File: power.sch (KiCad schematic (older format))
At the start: 23 parts, among them P1 CONN_01X02, P2 CONN_01X02, P23 CONN_01X02, P24 CONN_01X02, P3 CONN_01X02, P4 CONN_01X02, U1 ST1S14PHR

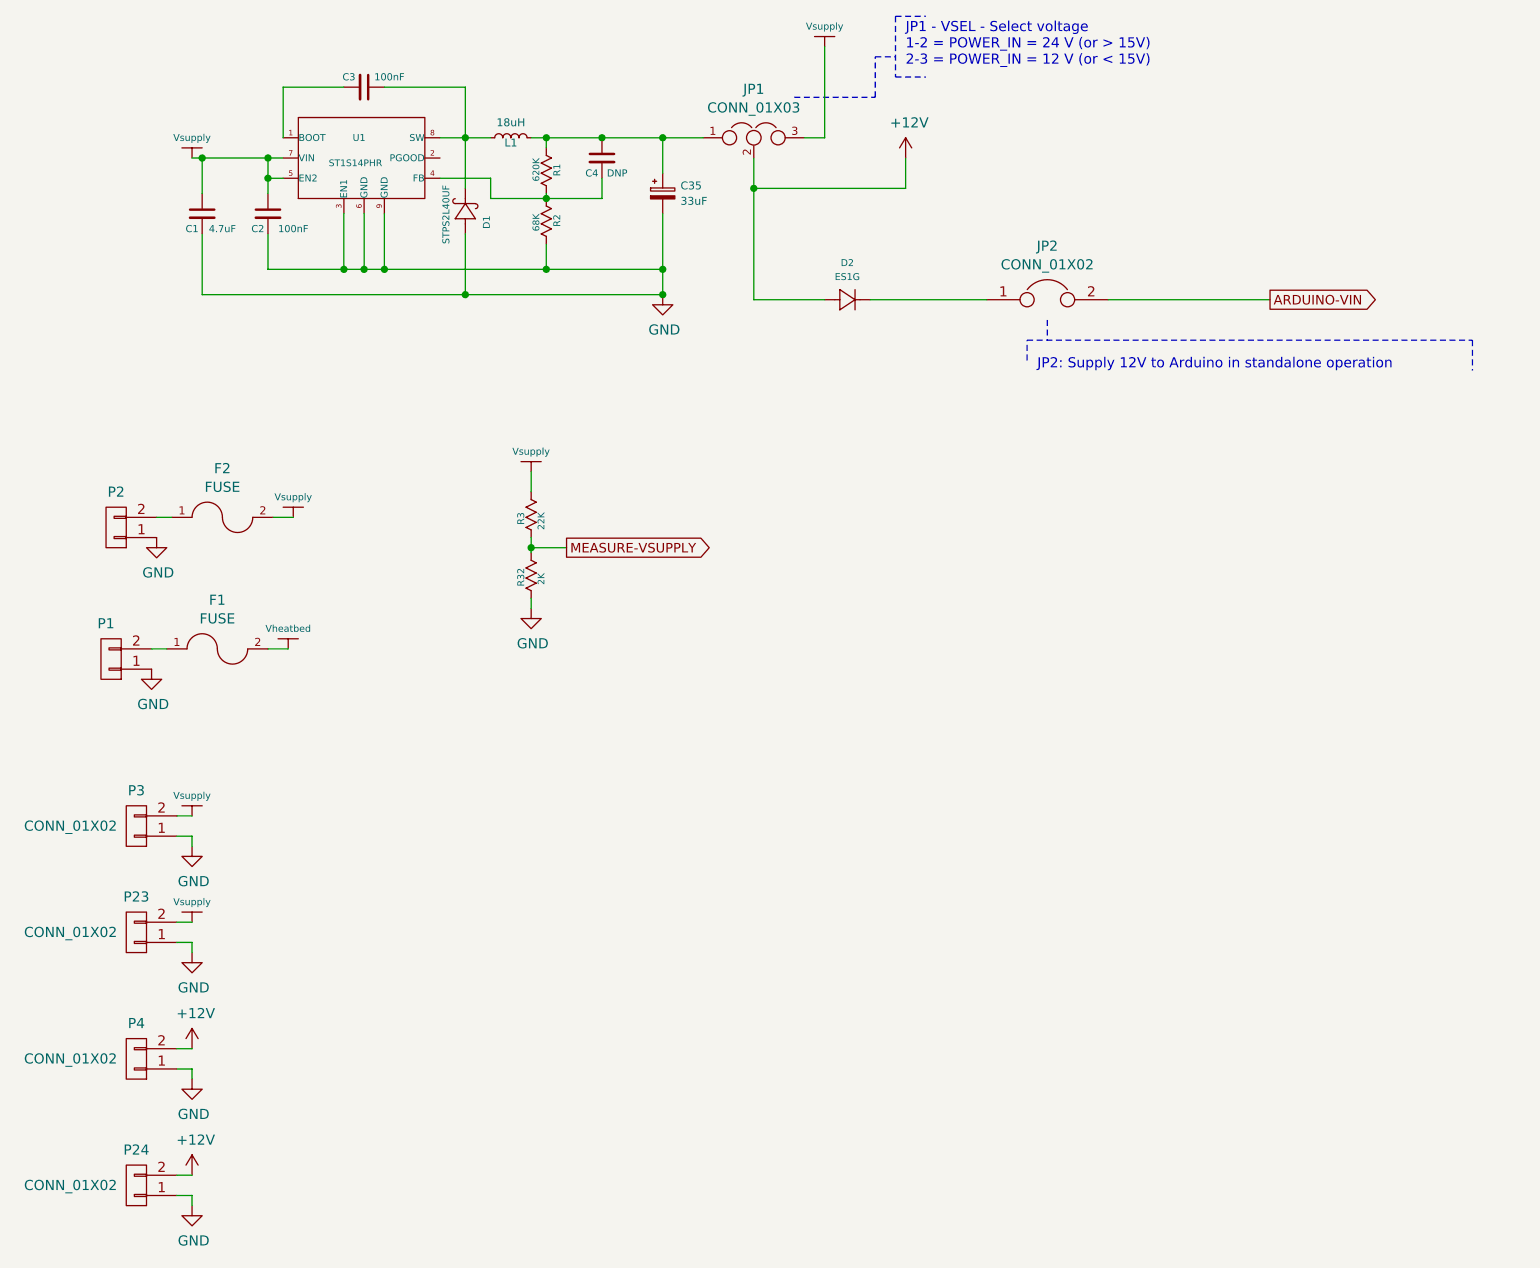
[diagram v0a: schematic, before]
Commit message: Removed jumper in arduino power line: arduino is now always powered when FireMC is powered
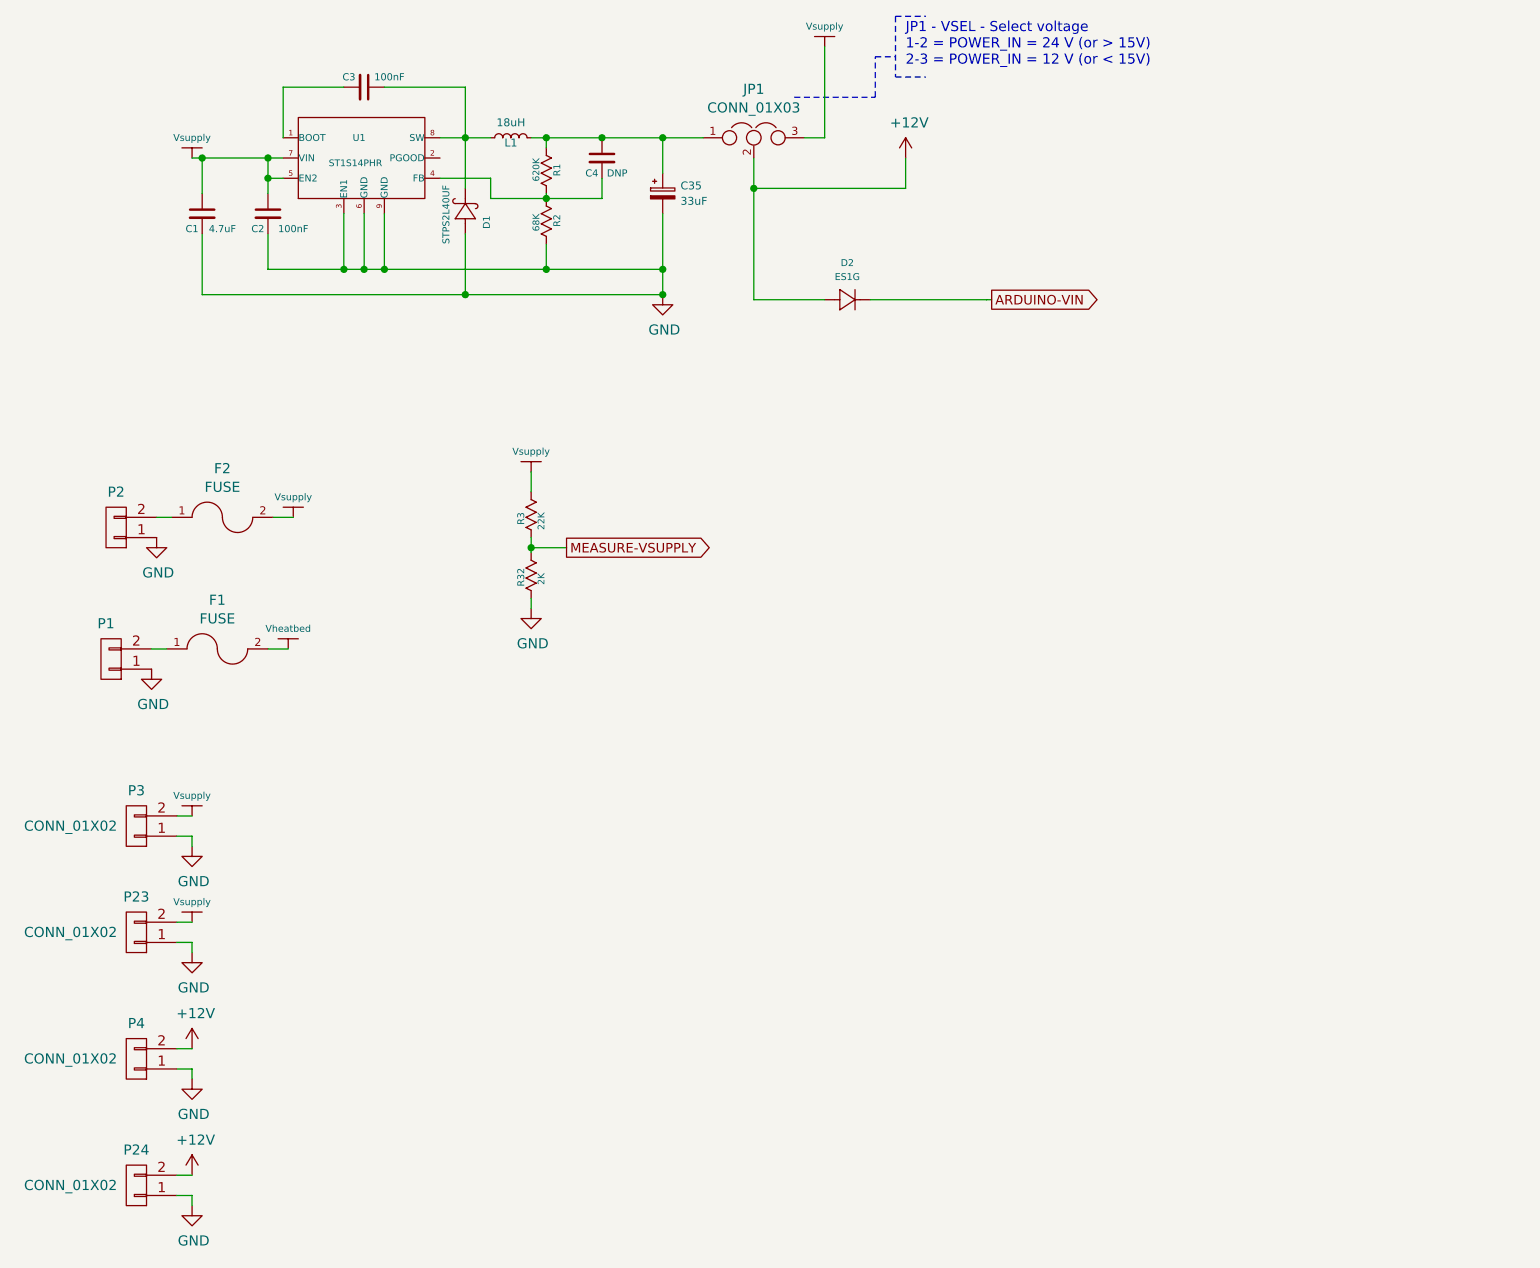
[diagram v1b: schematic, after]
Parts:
- removed JP2: CONN_01X02, headers:CON_HDR_1x2_2.54mm, symbol JUMPER
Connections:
- net ARDUINO-VIN: now also D2.1 (null)
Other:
- note removed: "JP2: Supply 12V to Arduino in standalone operation\n"
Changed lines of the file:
@@
 	5150 2075 4400 2075
 Wire Wire Line
-	6150 2625 6950 2625
+	5550 2625 5575 2625
 Wire Wire Line
 	5550 2625 4975 2625
@@
 Text Notes 5150 1475 0    50   ~ 0
 JP1 - VSEL - Select voltage\n1-2 = POWER_IN = 24 V (or > 15V)\n2-3 = POWER_IN = 12 V (or < 15V)
-Text GLabel 6950 2625 2    47   Output ~ 0
+Text GLabel 5575 2625 2    47   Output ~ 0
 ARDUINO-VIN
-Wire Notes Line
-	5850 2725 5850 2825
-Wire Notes Line
-	5750 2925 5750 2825
-Wire Notes Line
-	5750 2825 7950 2825
-Wire Notes Line
-	7950 2825 7950 2975
 Wire Notes Line
 	4600 1625 5000 1625
@@
 	5100 1525 5250 1525
 Wire Wire Line
-	4400 1925 4400 2625
+	4400 1925 4400 2075
+Wire Wire Line
+	4400 2075 4400 2625
 $Comp
 L STPS3L40UF D1
@@
 $EndComp
 Wire Wire Line
-	2975 1575 2975 2075
+	2975 1575 2975 1825
+Wire Wire Line
+	2975 1825 2975 2075
 Connection ~ 3375 1825
 $Comp
@@
 F 5 "ES1G" H 4750 2675 135 0001 L CNN "ManufacturerNo"
 	1    4750 2675
-	1    0    0    -1
-$EndComp
-$Comp
-L JUMPER JP2
-U 1 1 568ABCE3
-P 5850 2625
-F 0 "JP2" H 5850 2890 50  0000 C CNN
-F 1 "CONN_01X02" H 5850 2798 50  0000 C CNN
-F 2 "headers:CON_HDR_1x2_2.54mm" H 5850 2625 50  0001 C CNN
-F 3 "" H 5850 2625 50  0000 C CNN
-F 4 "BOARD_POWER" H 5850 2625 135 0001 L CNN "Comment"
-F 5 "2 pin 2.54mm pitch single row male header" H 5850 2625 135 0001 L CNN "Specification"
-	1    5850 2625
 	1    0    0    -1
 $EndComp
@@
 $EndComp
 Wire Wire Line
-	1625 1925 2075 1925
+	1625 1925 1675 1925
+Wire Wire Line
+	1675 1925 2000 1925
+Wire Wire Line
+	2000 1925 2075 1925
 $Comp
 L C_Small C3
@@
 $EndComp
 Wire Wire Line
-	2000 1925 2000 2100
+	2000 1925 2000 2025
+Wire Wire Line
+	2000 2025 2000 2100
 Connection ~ 2000 1925
 Wire Wire Line
-	3950 2600 1675 2600
+	3950 2600 2975 2600
+Wire Wire Line
+	2975 2600 1675 2600
 Wire Wire Line
 	2075 2025 2000 2025
@@
 	3375 1875 3375 1825
 Wire Wire Line
-	3100 2125 3650 2125
+	3100 2125 3375 2125
+Wire Wire Line
+	3375 2125 3650 2125
 Wire Wire Line
 	3100 2125 3100 2025
@@
 Connection ~ 3950 1825
 Wire Wire Line
-	3950 2200 3950 2600
+	3950 2200 3950 2475
+Wire Wire Line
+	3950 2475 3950 2600
 $Comp
 L C_Small C1
@@
 	2000 2300 2000 2475
 Wire Wire Line
-	2000 2475 3950 2475
+	2000 2475 2375 2475
+Wire Wire Line
+	2375 2475 2475 2475
+Wire Wire Line
+	2475 2475 2575 2475
+Wire Wire Line
+	2575 2475 3375 2475
+Wire Wire Line
+	3375 2475 3950 2475
 Connection ~ 3950 2475
 Wire Wire Line
@@
 $EndComp
 Wire Wire Line
-	2850 1825 3100 1825
-Wire Wire Line
-	3300 1825 4150 1825
-Text Notes 5800 2975 0    50   ~ 0
-JP2: Supply 12V to Arduino in standalone operation\n
+	2850 1825 2975 1825
+Wire Wire Line
+	2975 1825 3100 1825
+Wire Wire Line
+	3300 1825 3375 1825
+Wire Wire Line
+	3375 1825 3650 1825
+Wire Wire Line
+	3650 1825 3950 1825
+Wire Wire Line
+	3950 1825 4150 1825
 $Comp
 L Vsupply #P7
@@
 	3300 4150 3300 4100
 Wire Wire Line
-	3300 3875 3300 3800
+	3300 3875 3300 3850
+Wire Wire Line
+	3300 3850 3300 3800
 Wire Wire Line
 	3300 3575 3300 3475
